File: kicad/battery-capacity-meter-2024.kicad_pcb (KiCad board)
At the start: 2 copper layers, 100 x 99.9 mm, 77 parts, among them J3 Conn_MainBoard, J4 Conn_DisplayBoard, J5 PWR, Q1 2N3904, Q2 2N3906, Q3 2SD2390, Q6 X0402MF, SW1 CHARGE/DISCHARGE, SW2 1A MODE, U1 LM2596_StepDown_Module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

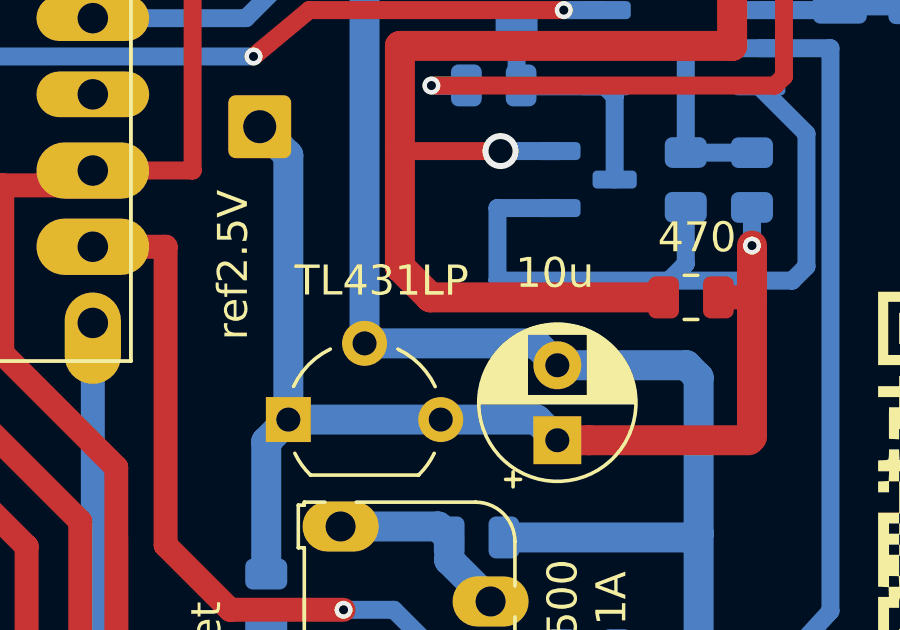
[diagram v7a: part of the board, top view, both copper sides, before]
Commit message: fix missing pcb track
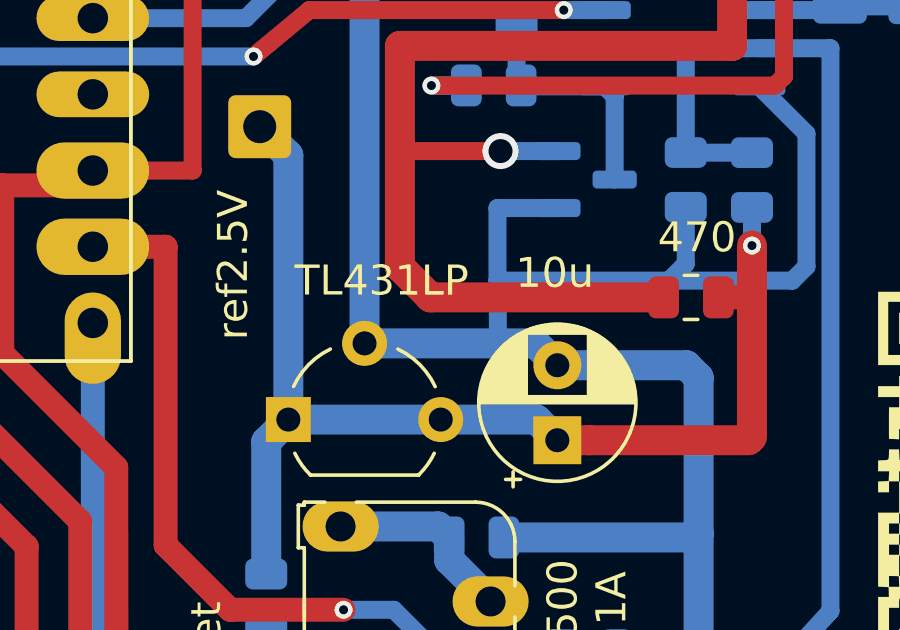
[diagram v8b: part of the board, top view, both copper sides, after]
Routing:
- net GND: track 389.1 -> 391.3 mm
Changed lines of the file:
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@@
   (segment (start 153.2382 64.9986) (end 151.349 64.9986) (width 0.6) (layer "B.Cu") (net 3))
   (segment (start 157.374688 95.8688) (end 158.1038 96.597912) (width 1) (layer "B.Cu") (net 3))
+  (segment (start 151.6776 95.8688) (end 156.3 95.8688) (width 1) (layer "B.Cu") (net 3))
   (segment (start 162.814 109.653512) (end 162.814 102.2096) (width 1) (layer "B.Cu") (net 3))
   (segment (start 110.452599 133.1478) (end 110.263287 132.958488) (width 1) (layer "B.Cu") (net 3))
@@
   (segment (start 133.1106 135.6868) (end 120.5676 135.6868) (width 1) (layer "B.Cu") (net 3))
   (segment (start 106.676253 132.5988) (end 103.617599 132.5988) (width 1) (layer "B.Cu") (net 3))
+  (segment (start 156.1211 93.7768) (end 156.1211 95.6899) (width 0.6) (layer "B.Cu") (net 3))
   (segment (start 157.226 77.9272) (end 161.036 77.9272) (width 1) (layer "B.Cu") (net 3))
   (segment (start 156.8958 78.2574) (end 157.226 77.9272) (width 1) (layer "B.Cu") (net 3))
   (segment (start 106.804946 132.5988) (end 106.676253 132.5988) (width 1) (layer "B.Cu") (net 3))
+  (segment (start 156.3 95.8688) (end 157.374688 95.8688) (width 1) (layer "B.Cu") (net 3))
   (segment (start 146.2532 69.9366) (end 154.4978 69.9366) (width 1.8) (layer "B.Cu") (net 3))
   (segment (start 155.9052 72.5443) (end 155.9052 70.4614) (width 0.6) (layer "B.Cu") (net 3))
@@
   (segment (start 156.3239 102.338312) (end 162.685288 102.338312) (width 1) (layer "B.Cu") (net 3))
   (segment (start 151.349 64.9986) (end 150.474001 64.9986) (width 0.6) (layer "B.Cu") (net 3))
+  (segment (start 156.1211 95.6899) (end 156.3 95.8688) (width 0.6) (layer "B.Cu") (net 3))
   (segment (start 106.649599 142.704801) (end 106.649599 132.754146) (width 1) (layer "B.Cu") (net 3))
   (segment (start 151.6776 83.4756) (end 156.8958 78.2574) (width 1) (layer "B.Cu") (net 3))
@@
   (segment (start 162.3847 93.2155) (end 161.8234 93.7768) (width 0.6) (layer "B.Cu") (net 3))
   (segment (start 151.349 67.5386) (end 153.543 67.5386) (width 0.6) (layer "B.Cu") (net 3))
-  (segment (start 151.6776 95.8688) (end 157.374688 95.8688) (width 1) (layer "B.Cu") (net 3))
   (segment (start 162.814 102.2096) (end 162.814 97.004312) (width 1) (layer "B.Cu") (net 3))
   (segment (start 164.8302 87.2998) (end 166.4082 88.8778) (width 0.6) (layer "B.Cu") (net 3))
